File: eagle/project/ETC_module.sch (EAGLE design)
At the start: 102 parts, among them IC1 LM358, Q2 MOSFET-PCHANNELFQP27P06, U1 V_REG_317SMD

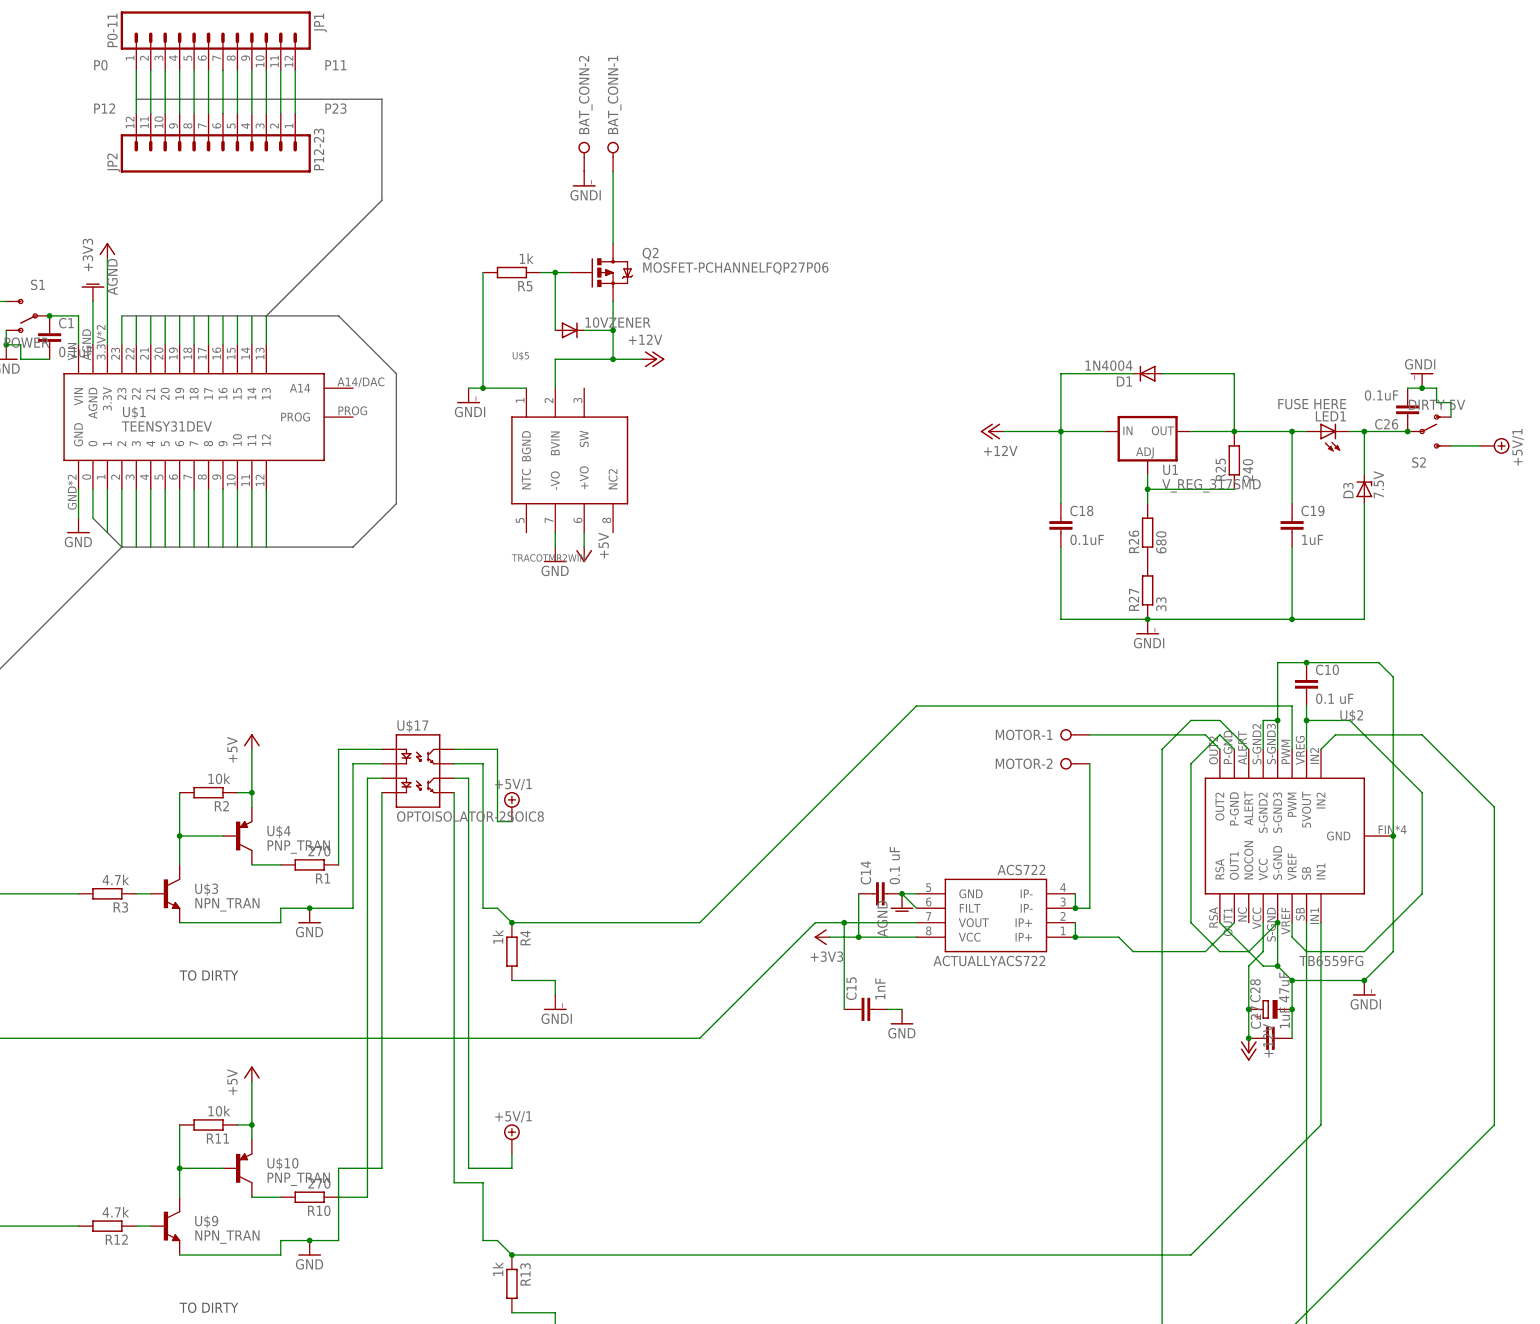
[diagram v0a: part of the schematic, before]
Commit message: Versions of the board which went to the fab house
Updating BOMS for component ordering
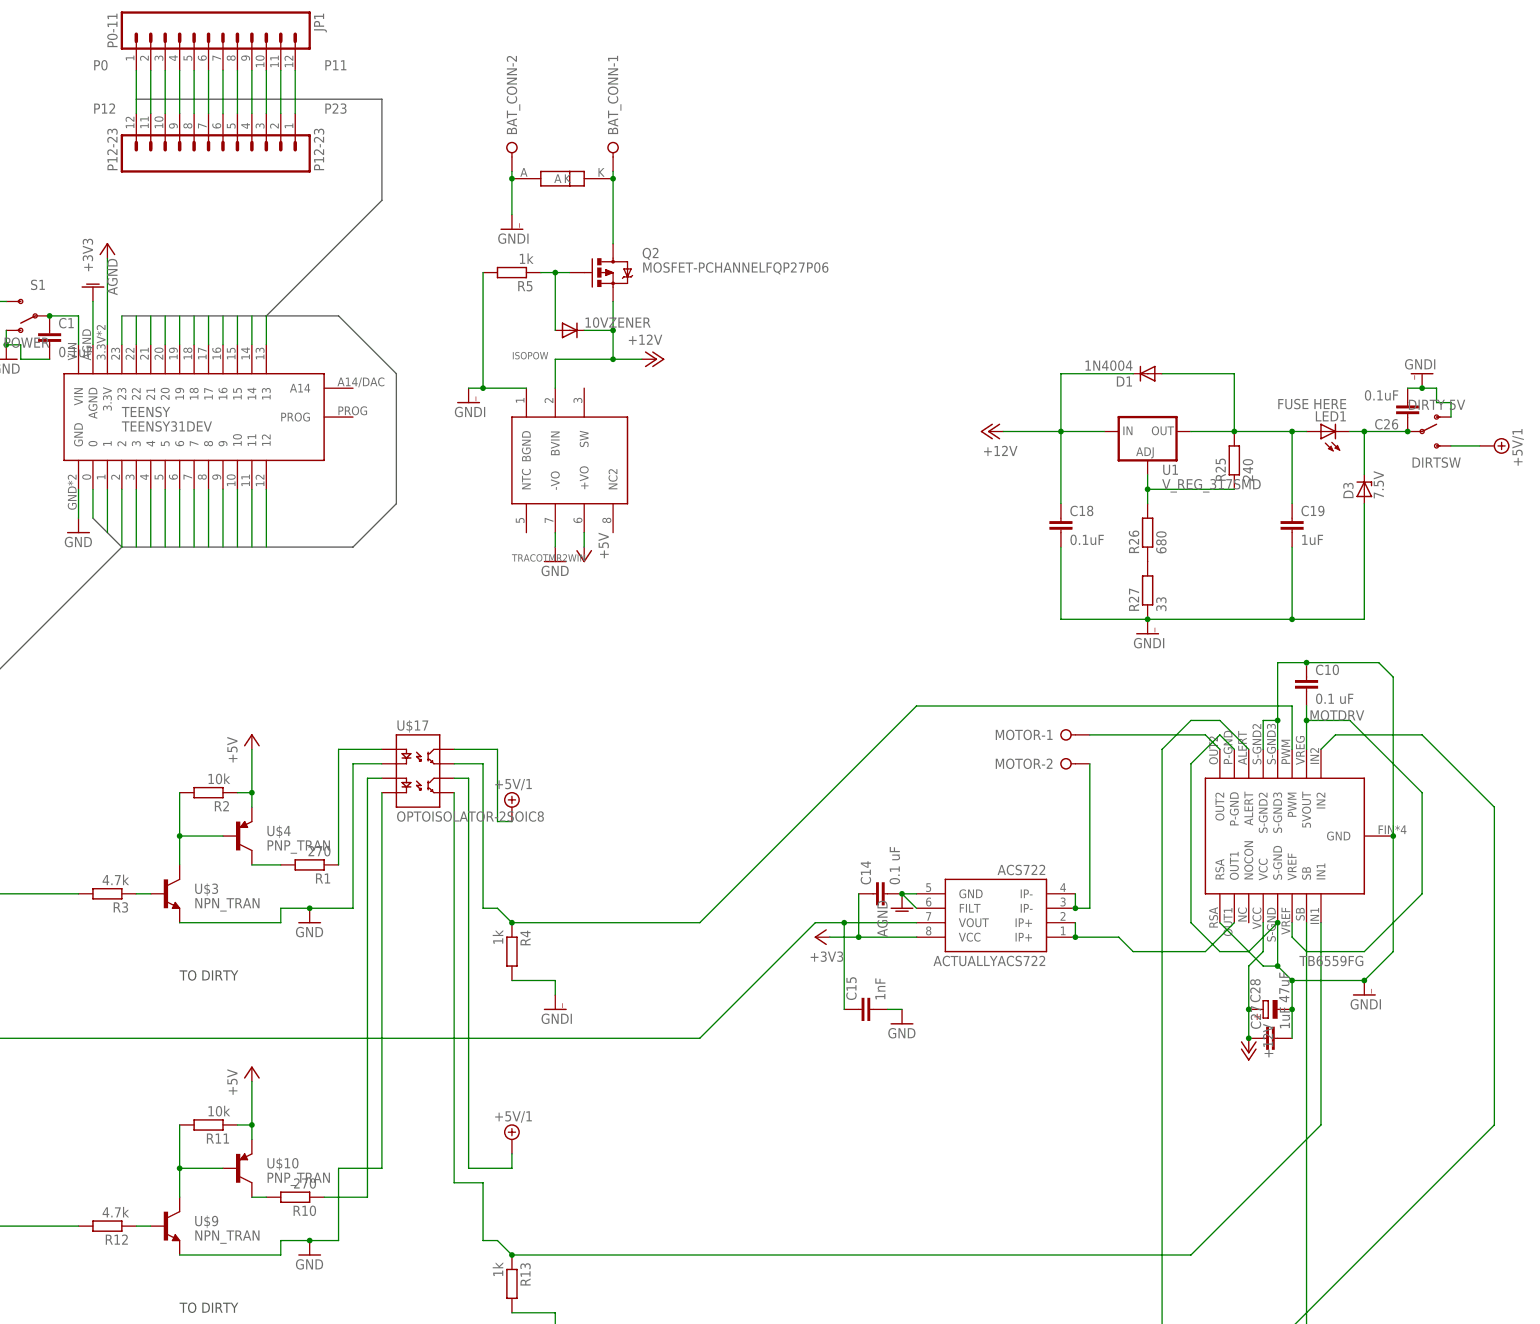
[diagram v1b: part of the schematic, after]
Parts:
- added TEENSY: TEENSY31DEV, custom:TEENSY31DEV
- U$1: value TEENSY31DEV -> LNBTVS; device custom:TEENSY31DEV -> custom:LNBTVS
- renumbered JP2 to P12-23, S2 to DIRTSW, U$2 to MOTDRV, U$5 to ISOPOW
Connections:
- net +3V3: now also TEENSY.3.3V; no longer U$1.3.3V
- net AGND: now also TEENSY.AGND; no longer U$1.AGND
- net GND: now also TEENSY.GND; no longer U$1.GND
- net GNDI: now also U$1.A
- net N$13: now also U$1.K
- net N$2: now also TEENSY.VIN; no longer U$1.VIN
- net P0: now also TEENSY.0; no longer U$1.0
- net P1: now also TEENSY.1; no longer U$1.1
- net P10: now also TEENSY.10; no longer U$1.10
- net P11: now also TEENSY.11; no longer U$1.11
- net P12: now also TEENSY.12; no longer U$1.12
- net P13: now also TEENSY.13; no longer U$1.13
- net P14: now also TEENSY.14; no longer U$1.14
- net P15: now also TEENSY.15; no longer U$1.15
- net P16: now also TEENSY.16; no longer U$1.16
- net P17: now also TEENSY.17; no longer U$1.17
- net P18: now also TEENSY.18; no longer U$1.18
- net P19: now also TEENSY.19; no longer U$1.19
- net P2: now also TEENSY.2; no longer U$1.2
- net P20: now also TEENSY.20; no longer U$1.20
- net P21: now also TEENSY.21; no longer U$1.21
- net P22: now also TEENSY.22; no longer U$1.22
- net P23: now also TEENSY.23; no longer U$1.23
- net P3: now also TEENSY.3; no longer U$1.3
- net P4: now also TEENSY.4; no longer U$1.4
- net P5: now also TEENSY.5; no longer U$1.5
- net P6: now also TEENSY.6; no longer U$1.6
- net P7: now also TEENSY.7; no longer U$1.7
- net P8: now also TEENSY.8; no longer U$1.8
- net P9: now also TEENSY.9; no longer U$1.9
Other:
- moved on the sheet: BAT_CONN-2, R10

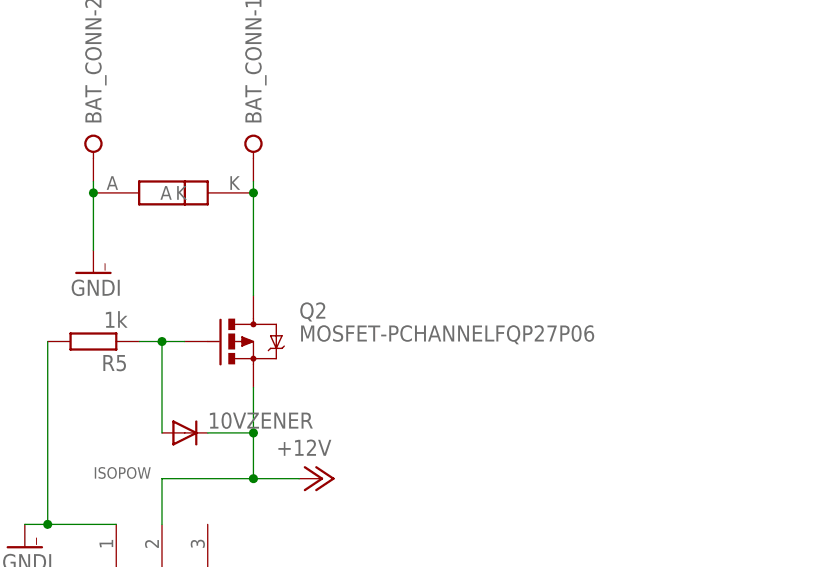
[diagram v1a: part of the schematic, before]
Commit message: update to fix reverse polarity protection
FLIP DS  on FET, only done on ETC schematic
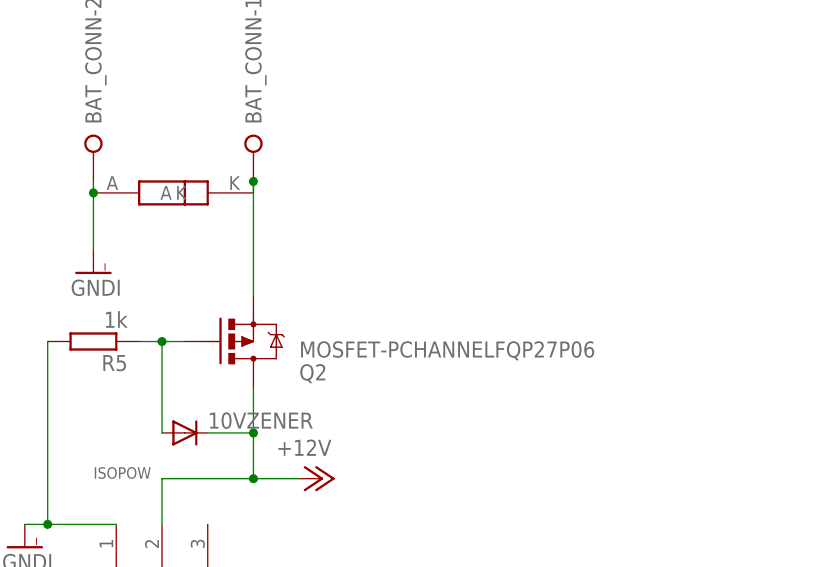
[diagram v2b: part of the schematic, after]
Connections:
- removed net N$13: BAT_CONN-1.KL, Q2.D, U$1.K
- new net N$58: BAT_CONN-1.KL, Q2.S, U$1.K
- net +12V: now also Q2.D; no longer Q2.S
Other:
- moved on the sheet: Q2
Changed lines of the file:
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@@
 <?xml version="1.0" encoding="utf-8"?>
 <!DOCTYPE eagle SYSTEM "eagle.dtd">
-<eagle version="7.3.0">
+<eagle version="7.4.0">
 <drawing>
 <settings>
@@
 <instance part="P+4" gate="1" x="10.16" y="-55.88"/>
 <instance part="GNDI2" gate="G$1" x="63.5" y="-104.14"/>
-<instance part="Q2" gate="G$1" x="73.66" y="25.4"/>
+<instance part="Q2" gate="G$1" x="73.66" y="25.4" rot="MR180"/>
 <instance part="10VZENER" gate="G$1" x="66.04" y="15.24"/>
 <instance part="R5" gate="G$1" x="55.88" y="25.4" rot="R180"/>
@@
 <net name="+12V" class="0">
 <segment>
-<pinref part="Q2" gate="G$1" pin="S"/>
-<wire x1="73.66" y1="20.32" x2="73.66" y2="15.24" width="0.1524" layer="91"/>
 <pinref part="10VZENER" gate="G$1" pin="C"/>
 <wire x1="73.66" y1="15.24" x2="68.58" y2="15.24" width="0.1524" layer="91"/>
@@
 <wire x1="73.66" y1="10.16" x2="78.74" y2="10.16" width="0.1524" layer="91"/>
 <pinref part="P+2" gate="1" pin="+12V"/>
+<junction x="73.66" y="10.16"/>
+<pinref part="Q2" gate="G$1" pin="D"/>
+<wire x1="73.66" y1="20.32" x2="73.66" y2="15.24" width="0.1524" layer="91"/>
 <junction x="73.66" y="15.24"/>
-<junction x="73.66" y="10.16"/>
 </segment>
 <segment>
@@
 <pinref part="U$6" gate="G$1" pin="B"/>
 <wire x1="66.04" y1="-317.5" x2="63.5" y2="-317.5" width="0.1524" layer="91"/>
-</segment>
-</net>
-<net name="N$13" class="0">
-<segment>
-<pinref part="BAT_CONN" gate="-1" pin="KL"/>
-<pinref part="Q2" gate="G$1" pin="D"/>
-<wire x1="73.66" y1="43.18" x2="73.66" y2="41.91" width="0.1524" layer="91"/>
-<pinref part="U$1" gate="G$1" pin="K"/>
-<wire x1="73.66" y1="41.91" x2="73.66" y2="30.48" width="0.1524" layer="91"/>
-<junction x="73.66" y="41.91"/>
 </segment>
 </net>
@@
 <segment>
 <pinref part="10VZENER" gate="G$1" pin="A"/>
-<pinref part="Q2" gate="G$1" pin="G"/>
 <pinref part="R5" gate="G$1" pin="1"/>
 <wire x1="60.96" y1="25.4" x2="63.5" y2="25.4" width="0.1524" layer="91"/>
-<wire x1="63.5" y1="25.4" x2="66.04" y2="25.4" width="0.1524" layer="91"/>
+<wire x1="63.5" y1="25.4" x2="63.5" y2="15.24" width="0.1524" layer="91"/>
+<pinref part="Q2" gate="G$1" pin="G"/>
+<wire x1="66.04" y1="25.4" x2="63.5" y2="25.4" width="0.1524" layer="91"/>
 <junction x="63.5" y="25.4"/>
-<wire x1="63.5" y1="25.4" x2="63.5" y2="15.24" width="0.1524" layer="91"/>
 </segment>
 </net>
@@
 </segment>
 </net>
+<net name="N$58" class="0">
+<segment>
+<pinref part="Q2" gate="G$1" pin="S"/>
+<wire x1="73.66" y1="43.18" x2="73.66" y2="30.48" width="0.1524" layer="91"/>
+<pinref part="BAT_CONN" gate="-1" pin="KL"/>
+<wire x1="73.66" y1="43.18" x2="73.66" y2="41.91" width="0.1524" layer="91"/>
+<pinref part="U$1" gate="G$1" pin="K"/>
+<junction x="73.66" y="43.18"/>
+</segment>
+</net>

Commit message: update before comp
Updates
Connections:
- net +12V: now also Q2.S; no longer Q2.D
- net N$58: now also Q2.D; no longer Q2.S
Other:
- moved on the sheet: Q2
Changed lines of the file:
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@@
 <instance part="P+4" gate="1" x="10.16" y="-55.88"/>
 <instance part="GNDI2" gate="G$1" x="63.5" y="-104.14"/>
-<instance part="Q2" gate="G$1" x="73.66" y="25.4" rot="MR180"/>
+<instance part="Q2" gate="G$1" x="73.66" y="25.4"/>
 <instance part="10VZENER" gate="G$1" x="66.04" y="15.24"/>
 <instance part="R5" gate="G$1" x="55.88" y="25.4" rot="R180"/>
@@
 <pinref part="P+2" gate="1" pin="+12V"/>
 <junction x="73.66" y="10.16"/>
-<pinref part="Q2" gate="G$1" pin="D"/>
+<pinref part="Q2" gate="G$1" pin="S"/>
 <wire x1="73.66" y1="20.32" x2="73.66" y2="15.24" width="0.1524" layer="91"/>
 <junction x="73.66" y="15.24"/>
@@
 <net name="N$58" class="0">
 <segment>
-<pinref part="Q2" gate="G$1" pin="S"/>
-<wire x1="73.66" y1="43.18" x2="73.66" y2="30.48" width="0.1524" layer="91"/>
 <pinref part="BAT_CONN" gate="-1" pin="KL"/>
 <wire x1="73.66" y1="43.18" x2="73.66" y2="41.91" width="0.1524" layer="91"/>
 <pinref part="U$1" gate="G$1" pin="K"/>
+<pinref part="Q2" gate="G$1" pin="D"/>
+<wire x1="73.66" y1="30.48" x2="73.66" y2="43.18" width="0.1524" layer="91"/>
 <junction x="73.66" y="43.18"/>
 </segment>
